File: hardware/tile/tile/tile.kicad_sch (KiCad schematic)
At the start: 0 parts

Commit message: init schematic for tile
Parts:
- added C1, C2: 0.1uF, Capacitor_SMD:C_0603_1608Metric, symbol Device:C
- added J1, J2, J3, J4: Conn_02x02_Row_Letter_Last, Connector_PinHeader_2.54mm:PinHeader_2x02_P2.54mm_Horizontal, symbol Connector_Generic:Conn_02x02_Row_Letter_Last
- added L1, L2, L3, L4, L5: L, symbol Device:L
- added Q1, Q2, Q3, Q4, Q5: AO3400A, Package_TO_SOT_SMD:SOT-23, symbol Transistor_FET:AO3400A
- added R1, R2, R3, R4, R5: 1R, Resistor_SMD:R_0201_0603Metric, symbol Device:R
- added U1: CH32V203C8T6, Package_QFP:LQFP-48_7x7mm_P0.5mm, symbol MCU_WCH_RiscV:CH32V203CxTx
- added U2: AMS1117-3.3, Package_TO_SOT_SMD:SOT-223-3_TabPin2, symbol Regulator_Linear:AMS1117-3.3
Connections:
- new net: L4.2, R4.1
- new net: Q1.3 (D), R1.2
- new net: Q3.3 (D), R3.2
- new net: Q5.3 (D), R5.2
- new net: Q2.3 (D), R2.2
- new net +3V3: C1.1, C2.1, U1.1 (VBAT), U1.24 (VDD_VIO), U1.36 (VDD), U1.48 (VDD), U1.9 (VDDA)
- new net +9V: L1.1, L2.1, L3.1, L4.1, L5.1
- new net ADC_IN0: L1.2, R1.1, U1.10 (PA0)
- new net ADC_IN1: L2.2, R2.1, U1.11 (PA1)
- new net ADC_IN4: L3.2, R3.1, U1.14 (PA4)
- new net ADC_IN5: Q4.3 (D), R4.2, U1.15 (PA5)
- new net ADC_IN6: L5.2, R5.1, U1.16 (PA6)
- new net COIL1: U1.39 (PB3)
- new net COIL2: U1.40 (PB4)
- new net COIL3: U1.41 (PB5)
- new net COIL4: U1.42 (PB6)
- new net COIL5: U1.43 (PB7)
- new net GND: C1.2, C2.2, Q1.2 (S), Q2.2 (S), Q3.2 (S), Q4.2 (S), Q5.2 (S), U1.23 (VSS), U1.35 (VSS), U1.47 (VSS), U1.8 (VSSA)
- new net SWCLK: U1.37 (SWCLK)
- new net SWDIO: U1.34 (SWDIO)
- new net USART1_RX: U1.31 (PA10)
- new net USART1_TX: U1.30 (PA9)
- new net USART2_RX: U1.13 (PA3)
- new net USART2_TX: U1.12 (PA2)
- new net USART3_RX: U1.22 (PB11)
- new net USART3_TX: U1.21 (PB10)
- new net USART4_RX: U1.19 (PB1)
- new net USART4_TX: U1.18 (PB0)

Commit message: tile schematic v1
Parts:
- removed J1, J2, J3, J4: Conn_02x02_Row_Letter_Last, Connector_PinHeader_2.54mm:PinHeader_2x02_P2.54mm_Horizontal, symbol Connector_Generic:Conn_02x02_Row_Letter_Last
- removed L1, L2, L3, L4, L5: L, symbol Device:L
- removed Q1, Q2, Q3, Q4, Q5: AO3400A, Package_TO_SOT_SMD:SOT-23, symbol Transistor_FET:AO3400A
- removed R1, R2, R3, R4, R5: 1R, Resistor_SMD:R_0201_0603Metric, symbol Device:R
- added C3, C6: 10uF, Capacitor_SMD:C_0603_1608Metric, symbol Device:C
- added C4, C5: 100nF, Capacitor_SMD:C_0603_1608Metric, symbol Device:C
- added D5, D6, D7, D8, D9: LED, LED_SMD:LED_0603_1608Metric, symbol Device:LED
- added R16, R17, R18, R19, R20: 330R, Resistor_SMD:R_0201_0603Metric, symbol Device:R
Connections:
- net +3V3: now also U2.2 (VO), C3.1, C4.1, R16.1
- net +9V: now also U2.3 (VI), C5.1, C6.1
- net GND: now also U2.1 (GND), C3.2, C4.2, C5.2, C6.2, D5.1 (K), D6.1 (K), D7.1 (K), D8.1 (K), D9.1 (K)
- net LED1: now reaches U1.25 (PB12)
- net LED1: now also R17.1
- net LED2: now reaches U1.26 (PB13)
- net LED2: now also R18.1
- net LED3: now reaches U1.27 (PB14)
- net LED3: now also R19.1
- net LED4: now reaches U1.28 (PB15)
- net LED4: now also R20.1
- new net: D7.2 (A), R18.2
- new net: D6.2 (A), R17.2
- new net: D5.2 (A), R16.2
- new net: D8.2 (A), R19.2
- new net: D9.2 (A), R20.2
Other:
- added sheet coil (coil.kicad_sch)
- added sheet coil1 (coil.kicad_sch)
- added sheet coil2 (coil.kicad_sch)
- added sheet coil3 (coil.kicad_sch)
- added sheet coil4 (coil.kicad_sch)
- added sheet connectors (connectors.kicad_sch)
- title: (none) -> F4io tile

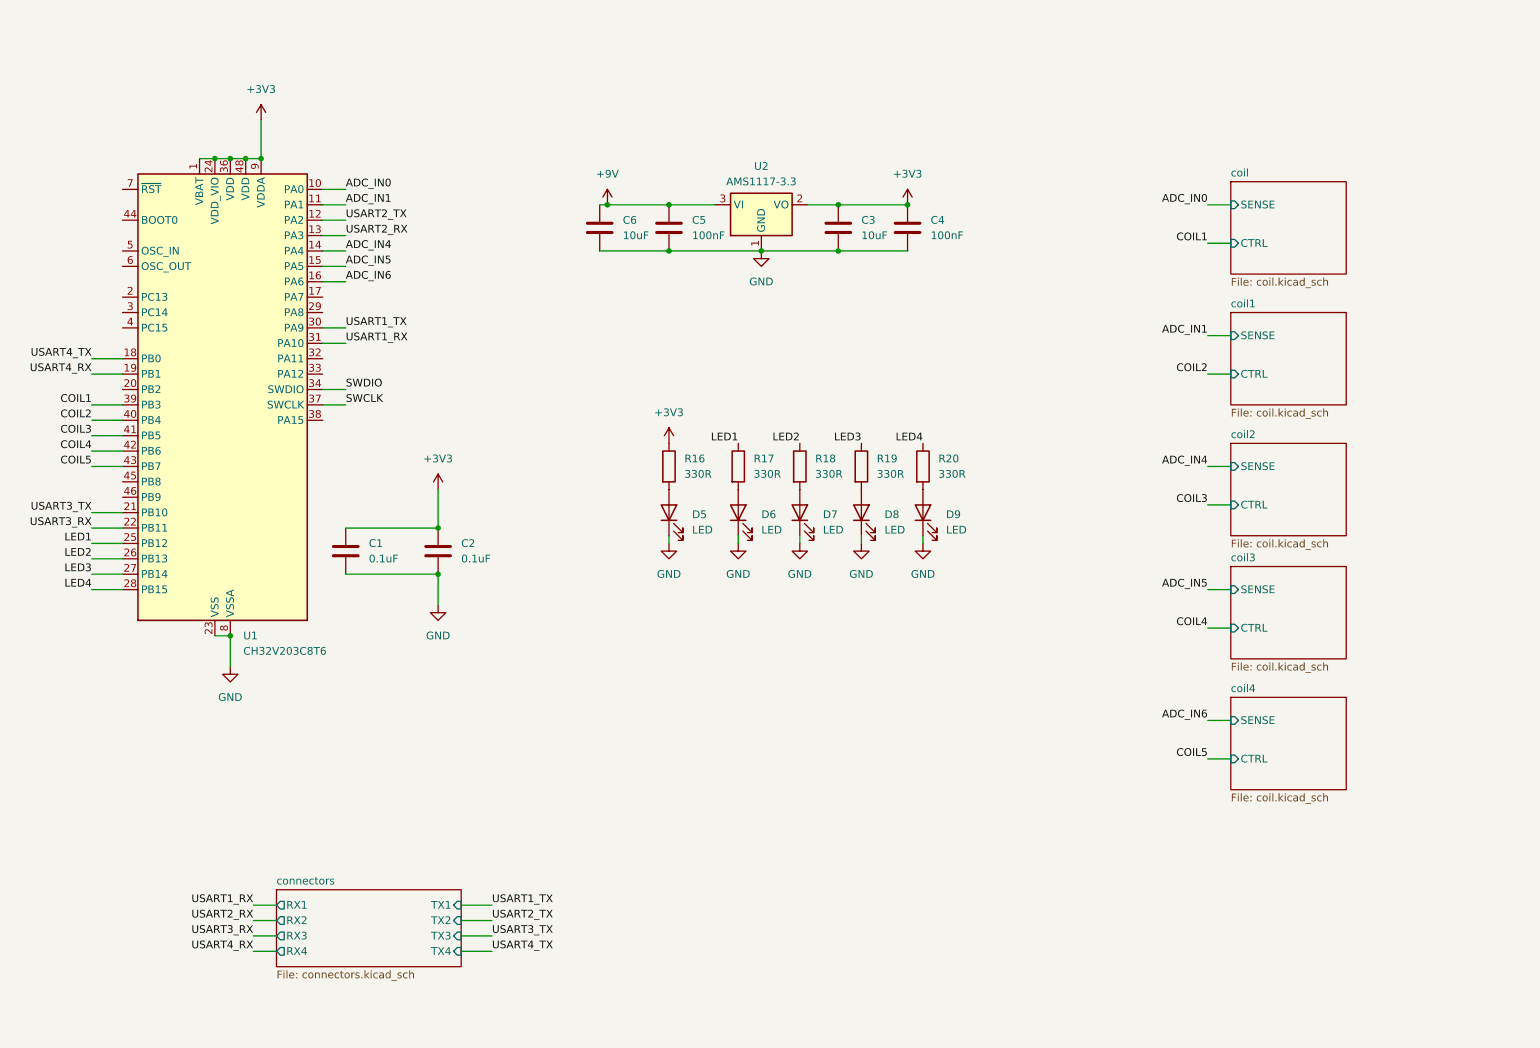
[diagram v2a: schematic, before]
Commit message: add debug, make tile schematic pretty
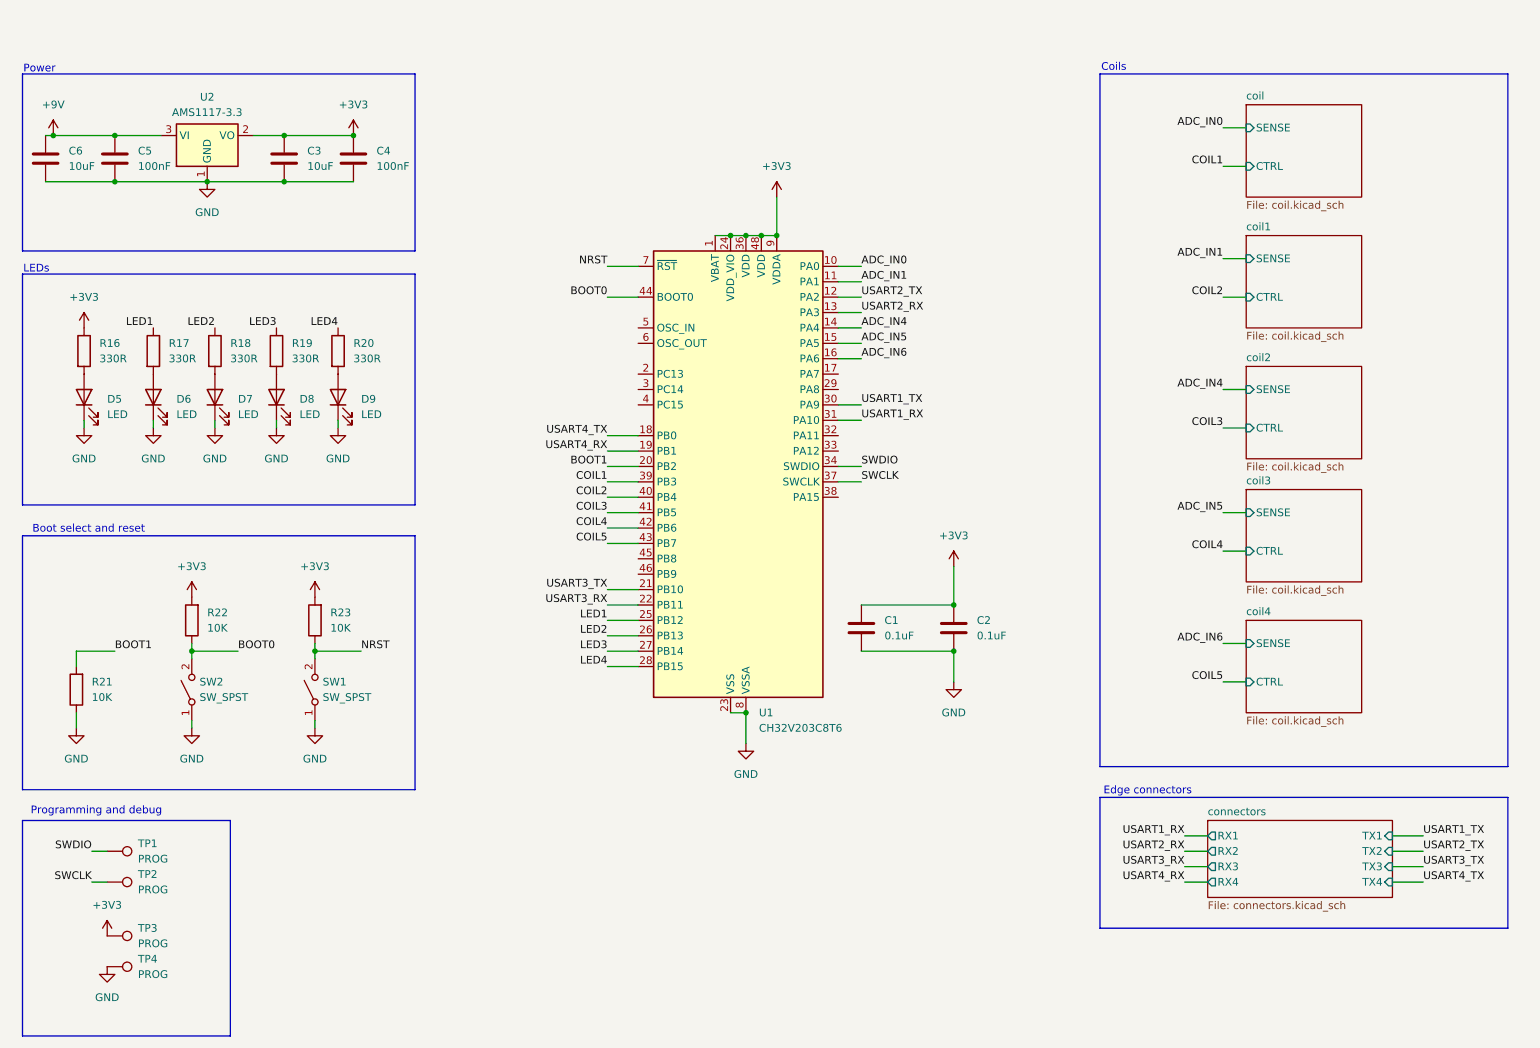
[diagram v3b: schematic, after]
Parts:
- added R21, R22, R23: 10K, symbol Device:R
- added SW1, SW2: SW_SPST, symbol Switch:SW_SPST
- added TP1, TP2, TP3, TP4: PROG, TestPoint:TestPoint_Pad_D1.5mm, symbol Connector:TestPoint
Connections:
- net +3V3: now also R22.2, R23.2, TP3.1
- net GND: now also R21.1, SW1.1 (A), SW2.1 (A), TP4.1
- net SWCLK: now also TP2.1
- net SWDIO: now also TP1.1
- net BOOT1: now reaches U1.20 (PB2)
- net BOOT1: now also R21.2
- net BOOT0: now reaches U1.44 (BOOT0)
- net BOOT0: now also R22.1, SW2.2 (B)
- net NRST: now reaches U1.7 (~{RST})
- net NRST: now also R23.1, SW1.2 (B)
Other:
- note added: "Boot select and reset"
- note added: "Coils"
- note added: "Edge connectors"
- note added: "LEDs"
- note added: "Power"
- note added: "Programming and debug"
- moved on the sheet: C1, C2, C3, C4, C5, C6, D5, D6, D7, D8, D9, R16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

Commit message: add vin sense to tile
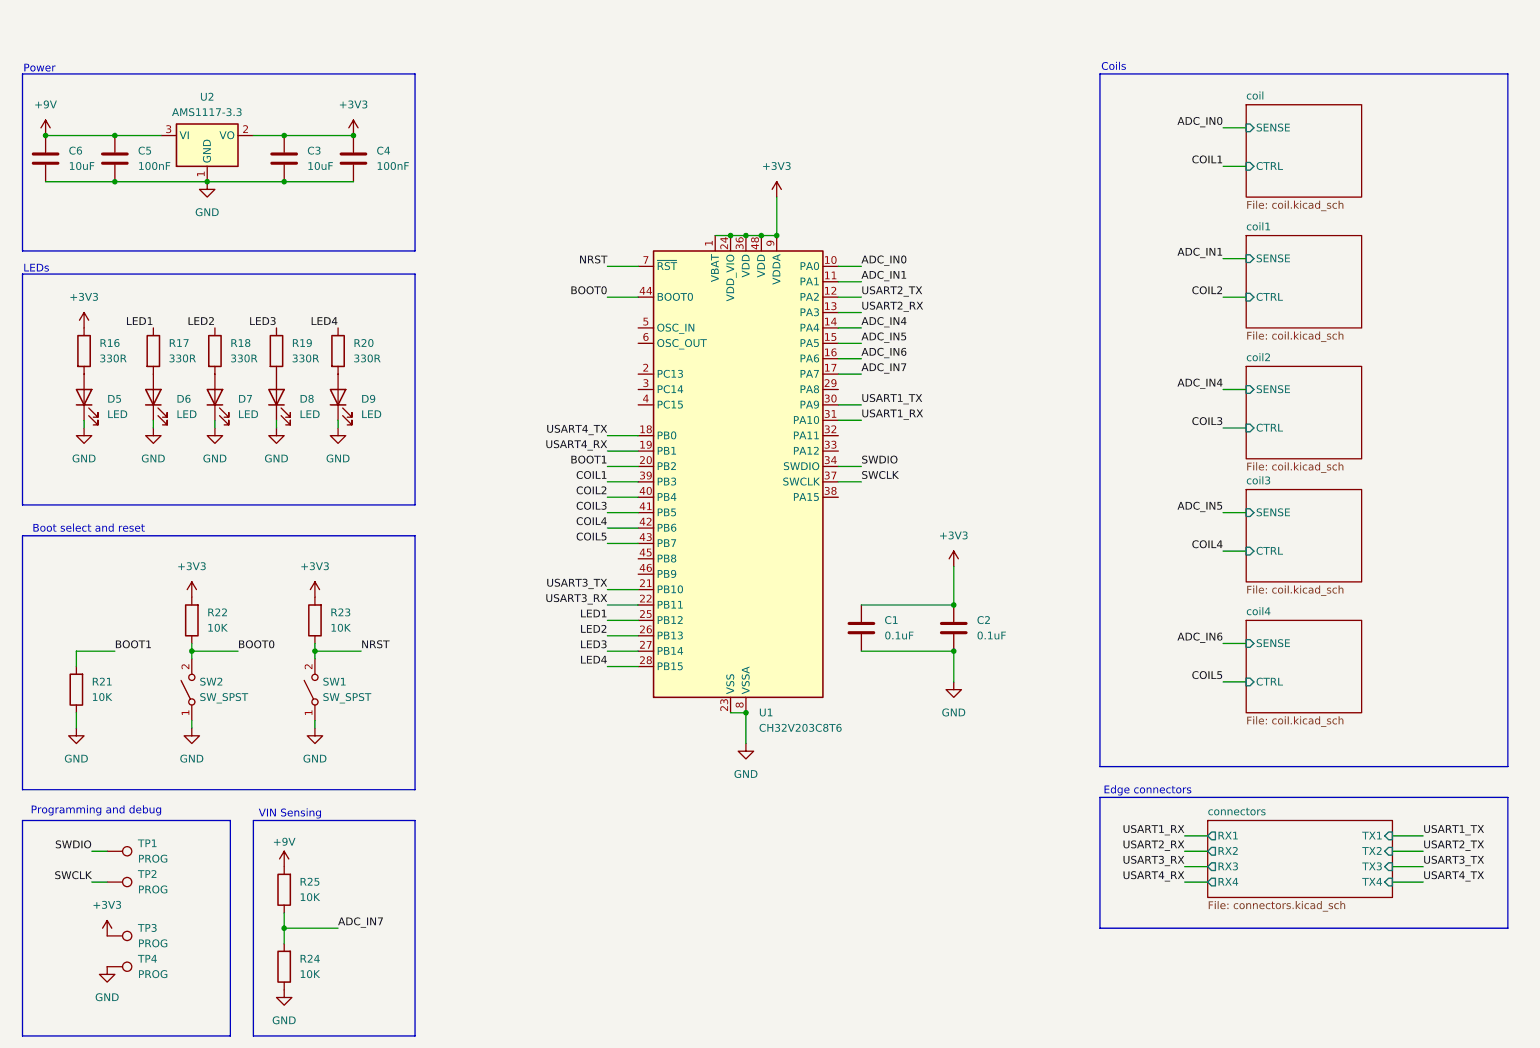
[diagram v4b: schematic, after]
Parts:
- added R24, R25: 10K, symbol Device:R
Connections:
- net +9V: now also R25.2
- net GND: now also R24.1
- net ADC_IN7: now reaches U1.17 (PA7)
- net ADC_IN7: now also R24.2, R25.1
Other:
- note added: "VIN Sensing"

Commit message: fix tile sense resistors
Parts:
- R24: value 10K -> 100K
- R25: value 10K -> 220K
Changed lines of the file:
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@@
 			)
 		)
-		(property "Value" "10K"
+		(property "Value" "100K"
 			(at 77.47 170.1799 0)
 			(effects
@@
 			)
 		)
-		(property "Value" "10K"
+		(property "Value" "220K"
 			(at 77.47 157.4799 0)
 			(effects

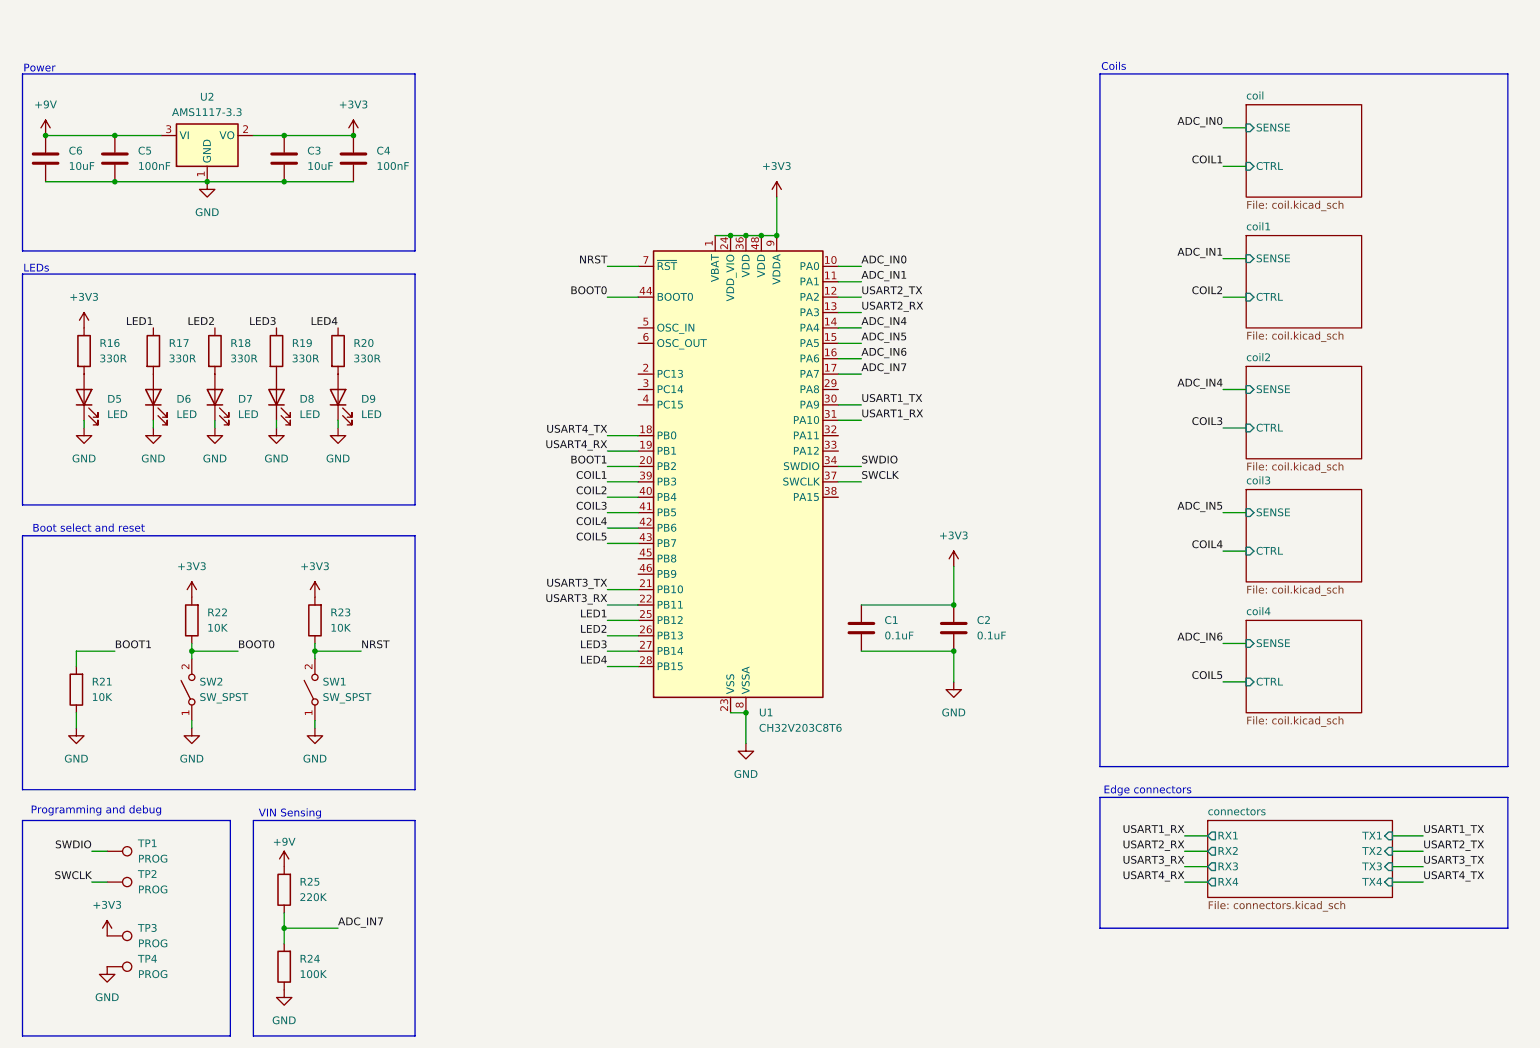
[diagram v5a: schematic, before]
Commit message: added coils will improve them later
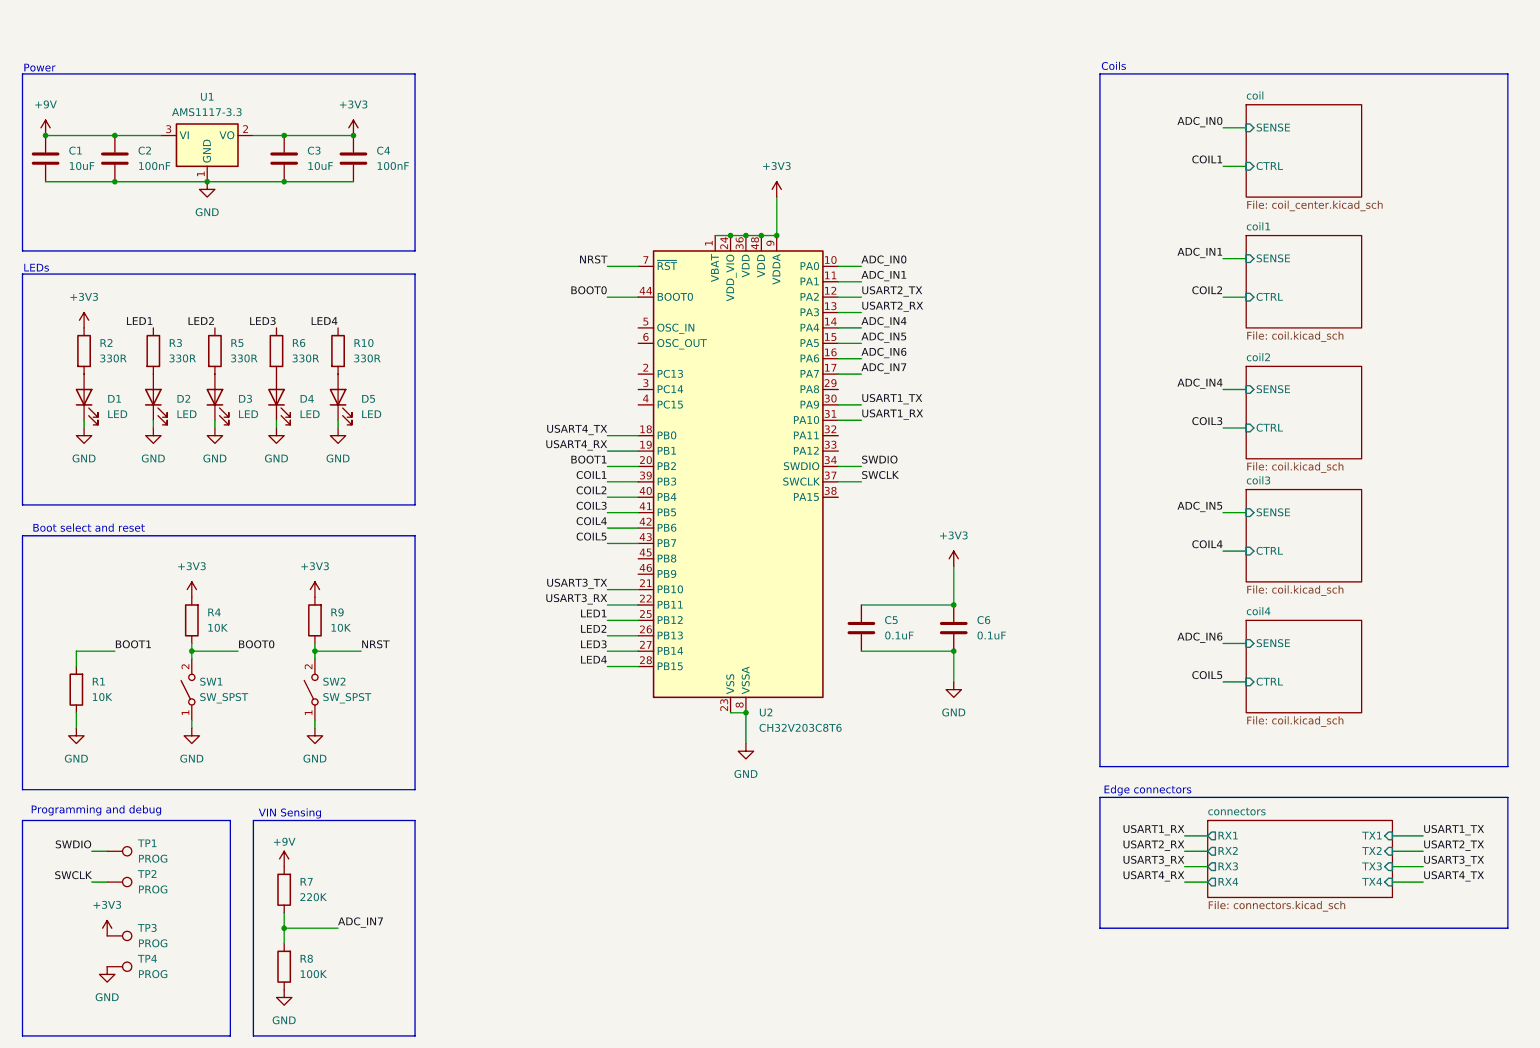
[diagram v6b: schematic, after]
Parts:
- R1: renamed from R21; footprint (none) -> Resistor_SMD:R_0402_1005Metric
- R4: renamed from R22; footprint (none) -> Resistor_SMD:R_0402_1005Metric
- R7: renamed from R25; footprint (none) -> Resistor_SMD:R_0402_1005Metric
- R8: renamed from R24; footprint (none) -> Resistor_SMD:R_0402_1005Metric
- R9: renamed from R23; footprint (none) -> Resistor_SMD:R_0402_1005Metric
- renumbered C6 to C1, C5 to C2, C1 to C5, C2 to C6, D5 to D1, D6 to D2, D7 to D3, D8 to D4, D9 to D5, R20 to R10, R16 to R2, R17 to R3, R18 to R5, R19 to R6, SW2 to SW1, SW1 to SW2, U2 to U1, U1 to U2
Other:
- sheet coil: file coil.kicad_sch -> coil_center.kicad_sch
